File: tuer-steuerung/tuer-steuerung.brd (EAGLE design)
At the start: 65.7 x 67.3 mm, 47 parts, among them IC1 L6203, IC2 MEGA8-P, Q1 16Mhz, T1 BC337, T2 BC337

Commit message: Letzte Anpassungen vor dem Ätzen
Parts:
- removed R10, R9: (no value), resistor:0207/2V
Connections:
- removed net N$12: R9.2, U$4.1
- removed net N$14: R10.2, U$4.3
- net N$11: now also U$4.1; no longer R9.1
- net N$13: now also U$4.3; no longer R10.1
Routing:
- net N$12: track 6.88 -> 0.00 mm
- net N$13: track 3.81 -> 10.7 mm
- net N$11: track 4.34 -> 11.2 mm
- net N$14: track 6.65 -> 0.00 mm
- net VCC: track 248.1 -> 250.5 mm
- net DOORSTATE: track 81.0 -> 82.5 mm
- net SET_CLOSE: track 39.5 -> 40.2 mm
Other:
- board text added: "netz39"

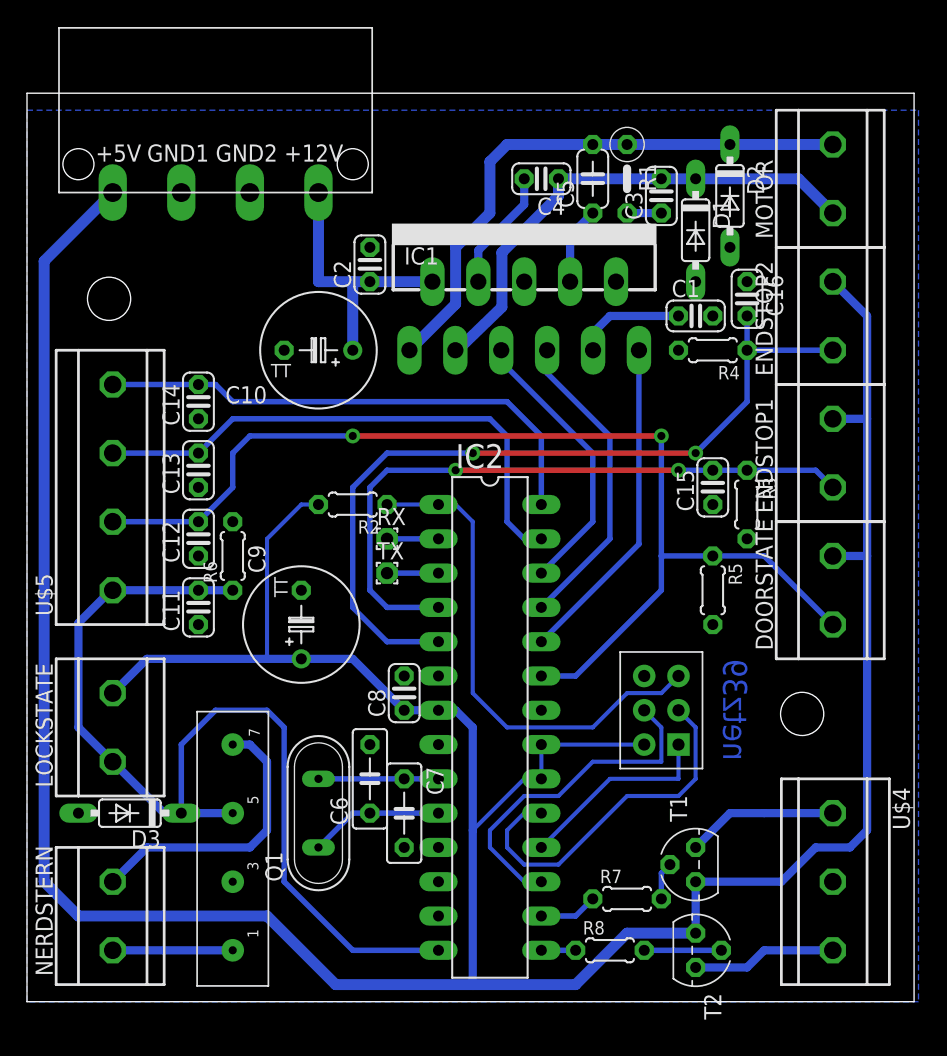
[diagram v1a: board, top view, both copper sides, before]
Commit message: andere Holes, Beschriftung, eine Leiterbahn leicht verschoben
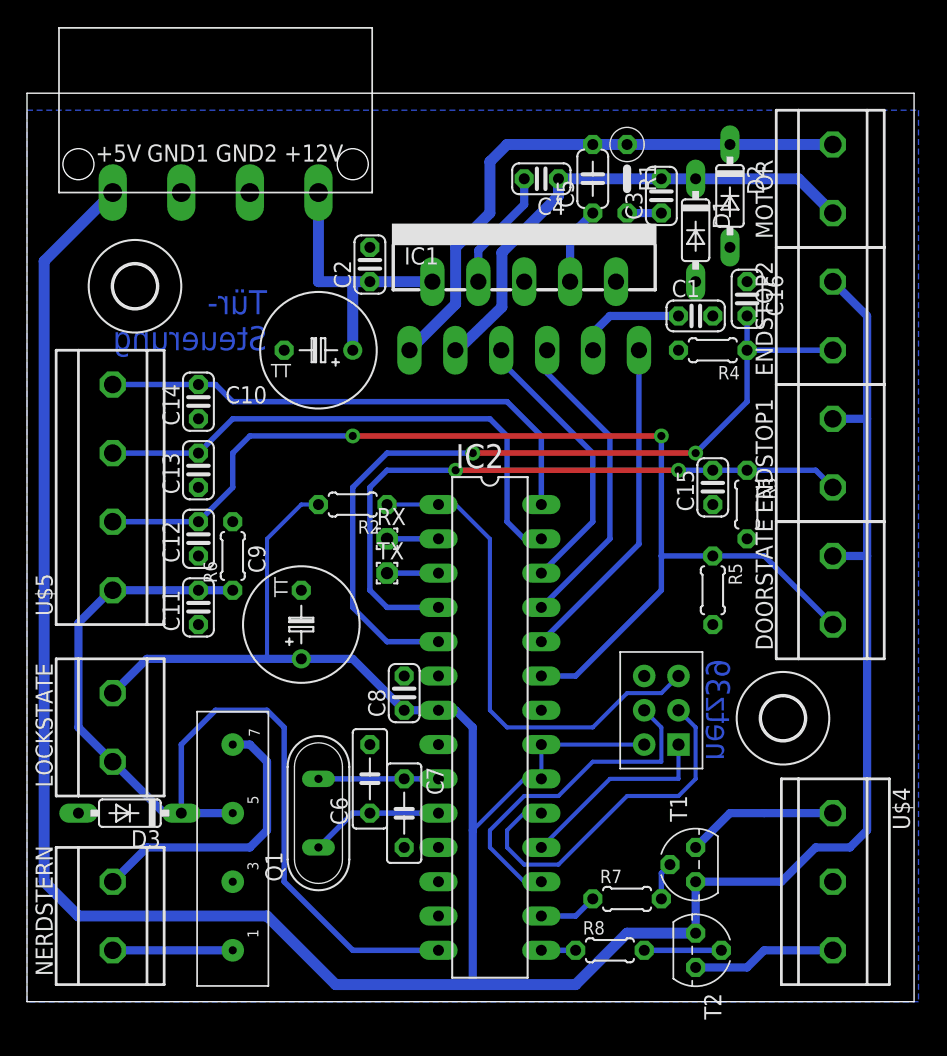
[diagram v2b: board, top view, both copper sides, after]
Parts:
- added U$6, U$7: (no value), holes:3,2
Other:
- board text added: "Tür- Steuerung"
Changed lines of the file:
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@@
 <grid distance="1.27" unitdist="mm" unit="mm" style="lines" multiple="1" display="no" altdistance="0.025" altunitdist="inch" altunit="inch"/>
 <layers>
-<layer number="1" name="Top" color="4" fill="1" visible="yes" active="yes"/>
+<layer number="1" name="Top" color="4" fill="1" visible="no" active="yes"/>
 <layer number="16" name="Bottom" color="1" fill="1" visible="yes" active="yes"/>
 <layer number="17" name="Pads" color="2" fill="1" visible="yes" active="yes"/>
 <layer number="18" name="Vias" color="2" fill="1" visible="yes" active="yes"/>
-<layer number="19" name="Unrouted" color="6" fill="1" visible="yes" active="yes"/>
+<layer number="19" name="Unrouted" color="6" fill="1" visible="no" active="yes"/>
 <layer number="20" name="Dimension" color="15" fill="1" visible="yes" active="yes"/>
-<layer number="21" name="tPlace" color="7" fill="1" visible="yes" active="yes"/>
-<layer number="22" name="bPlace" color="7" fill="1" visible="yes" active="yes"/>
-<layer number="23" name="tOrigins" color="15" fill="1" visible="yes" active="yes"/>
-<layer number="24" name="bOrigins" color="15" fill="1" visible="yes" active="yes"/>
-<layer number="25" name="tNames" color="7" fill="1" visible="yes" active="yes"/>
-<layer number="26" name="bNames" color="7" fill="1" visible="yes" active="yes"/>
-<layer number="27" name="tValues" color="7" fill="1" visible="yes" active="yes"/>
-<layer number="28" name="bValues" color="7" fill="1" visible="yes" active="yes"/>
+<layer number="21" name="tPlace" color="7" fill="1" visible="no" active="yes"/>
+<layer number="22" name="bPlace" color="7" fill="1" visible="no" active="yes"/>
+<layer number="23" name="tOrigins" color="15" fill="1" visible="no" active="yes"/>
+<layer number="24" name="bOrigins" color="15" fill="1" visible="no" active="yes"/>
+<layer number="25" name="tNames" color="7" fill="1" visible="no" active="yes"/>
+<layer number="26" name="bNames" color="7" fill="1" visible="no" active="yes"/>
+<layer number="27" name="tValues" color="7" fill="1" visible="no" active="yes"/>
+<layer number="28" name="bValues" color="7" fill="1" visible="no" active="yes"/>
 <layer number="29" name="tStop" color="7" fill="3" visible="no" active="yes"/>
 <layer number="30" name="bStop" color="7" fill="6" visible="no" active="yes"/>
@@
 <layer number="43" name="vRestrict" color="2" fill="10" visible="no" active="yes"/>
 <layer number="44" name="Drills" color="7" fill="1" visible="no" active="yes"/>
-<layer number="45" name="Holes" color="7" fill="1" visible="no" active="yes"/>
+<layer number="45" name="Holes" color="7" fill="1" visible="yes" active="yes"/>
 <layer number="46" name="Milling" color="3" fill="1" visible="no" active="yes"/>
 <layer number="47" name="Measures" color="7" fill="1" visible="no" active="yes"/>
@@
 <layer number="49" name="Reference" color="7" fill="1" visible="no" active="yes"/>
 <layer number="50" name="dxf" color="7" fill="1" visible="no" active="no"/>
-<layer number="51" name="tDocu" color="7" fill="1" visible="no" active="yes"/>
-<layer number="52" name="bDocu" color="7" fill="1" visible="no" active="yes"/>
+<layer number="51" name="tDocu" color="7" fill="1" visible="yes" active="yes"/>
+<layer number="52" name="bDocu" color="7" fill="1" visible="yes" active="yes"/>
 <layer number="91" name="Nets" color="2" fill="1" visible="no" active="no"/>
 <layer number="92" name="Busses" color="1" fill="1" visible="no" active="no"/>
@@
 <wire x1="65.71" y1="67.3" x2="0" y2="67.3" width="0" layer="20"/>
 <wire x1="0" y1="67.3" x2="0" y2="0" width="0" layer="20"/>
-<hole x="57.42" y="21.32" drill="3.2"/>
-<hole x="6.08" y="52.07" drill="3.2"/>
-<text x="53.34" y="25.4" size="1.778" layer="16" font="vector" rot="MR270">netz39</text>
+<text x="52.07" y="25.4" size="1.778" layer="16" font="vector" rot="MR270">netz39</text>
+<text x="17.78" y="48.26" size="1.778" layer="16" font="vector" rot="MR0">Tür-
+Steuerung</text>
 </plain>
 <attributes>
@@
 <attribute name="REICHELT" value="AKL 101-04" x="6.35" y="38.1" size="1.778" layer="27" rot="R90" display="off"/>
 </element>
+<element name="U$6" library="holes" package="3,2" value="" x="8" y="53"/>
+<element name="U$7" library="holes" package="3,2" value="" x="56" y="21"/>
 </elements>
 <signals>
@@
 <contactref element="IC2" pad="1"/>
 <contactref element="U$3" pad="RST"/>
-<wire x1="35.56" y1="20.32" x2="33.02" y2="22.86" width="0.3048" layer="16"/>
-<wire x1="33.02" y1="22.86" x2="33.02" y2="35.56" width="0.3048" layer="16"/>
+<wire x1="35.56" y1="20.32" x2="34.29" y2="21.59" width="0.3048" layer="16"/>
+<wire x1="34.29" y1="21.59" x2="34.29" y2="34.29" width="0.3048" layer="16"/>
 <wire x1="35.56" y1="20.32" x2="41.91" y2="20.32" width="0.3048" layer="16"/>
 <wire x1="41.91" y1="20.32" x2="44.45" y2="22.86" width="0.3048" layer="16"/>
@@
 <wire x1="46.99" y1="22.86" x2="48.26" y2="24.13" width="0.3048" layer="16"/>
 <wire x1="26.67" y1="36.83" x2="30.48" y2="36.83" width="0.3048" layer="16"/>
-<wire x1="33.02" y1="35.56" x2="31.75" y2="36.83" width="0.3048" layer="16"/>
+<wire x1="34.29" y1="34.29" x2="31.75" y2="36.83" width="0.3048" layer="16"/>
 <wire x1="31.75" y1="36.83" x2="30.48" y2="36.83" width="0.3048" layer="16"/>
 </signal>
@@
 </board>
 </drawing>
+<compatibility>
+<note version="6.3" minversion="6.2.2" severity="warning">
+Since Version 6.2.2 text objects can contain more than one line,
+which will not be processed correctly with this version.
+</note>
+</compatibility>
 </eagle>
